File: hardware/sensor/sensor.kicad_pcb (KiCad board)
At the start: 2 copper layers, 88.9 x 68.6 mm, 12 parts

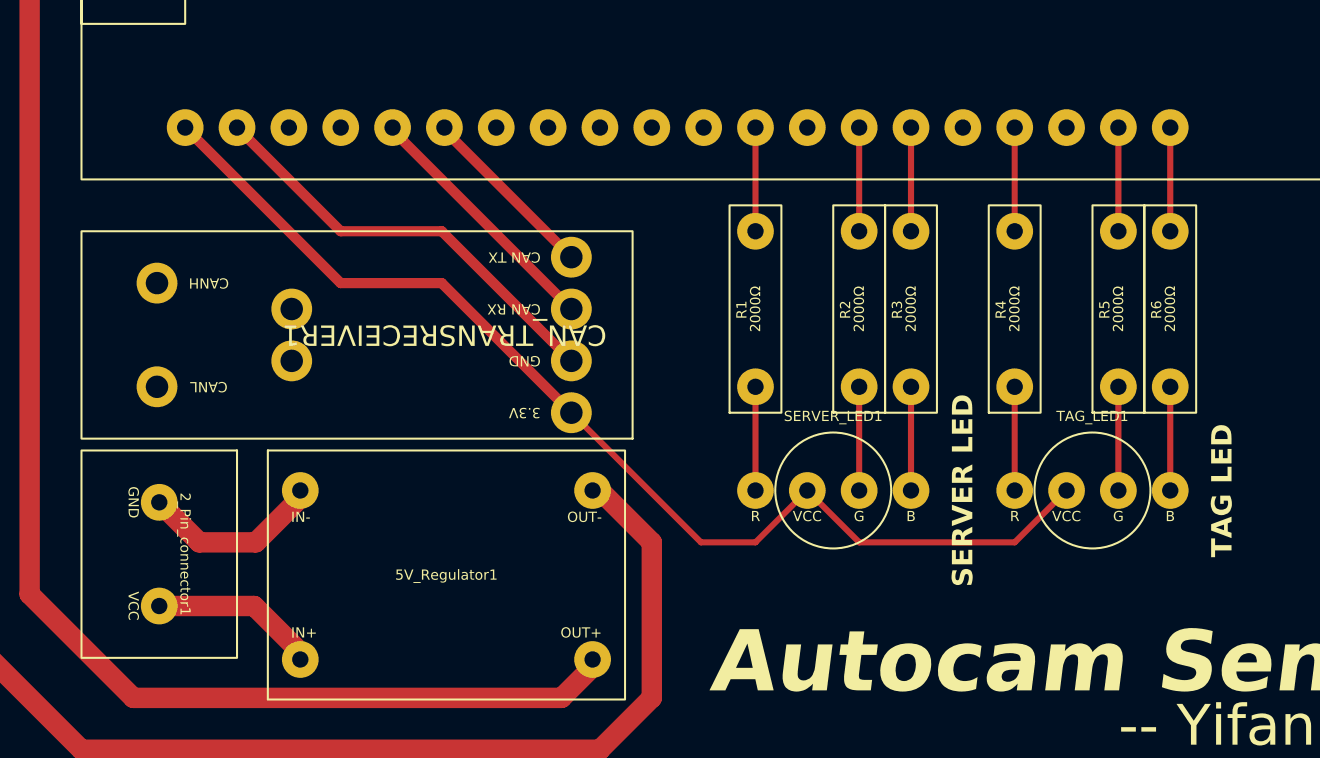
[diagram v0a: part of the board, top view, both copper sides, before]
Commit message: KiCad footprint library: Refactor footprint names.
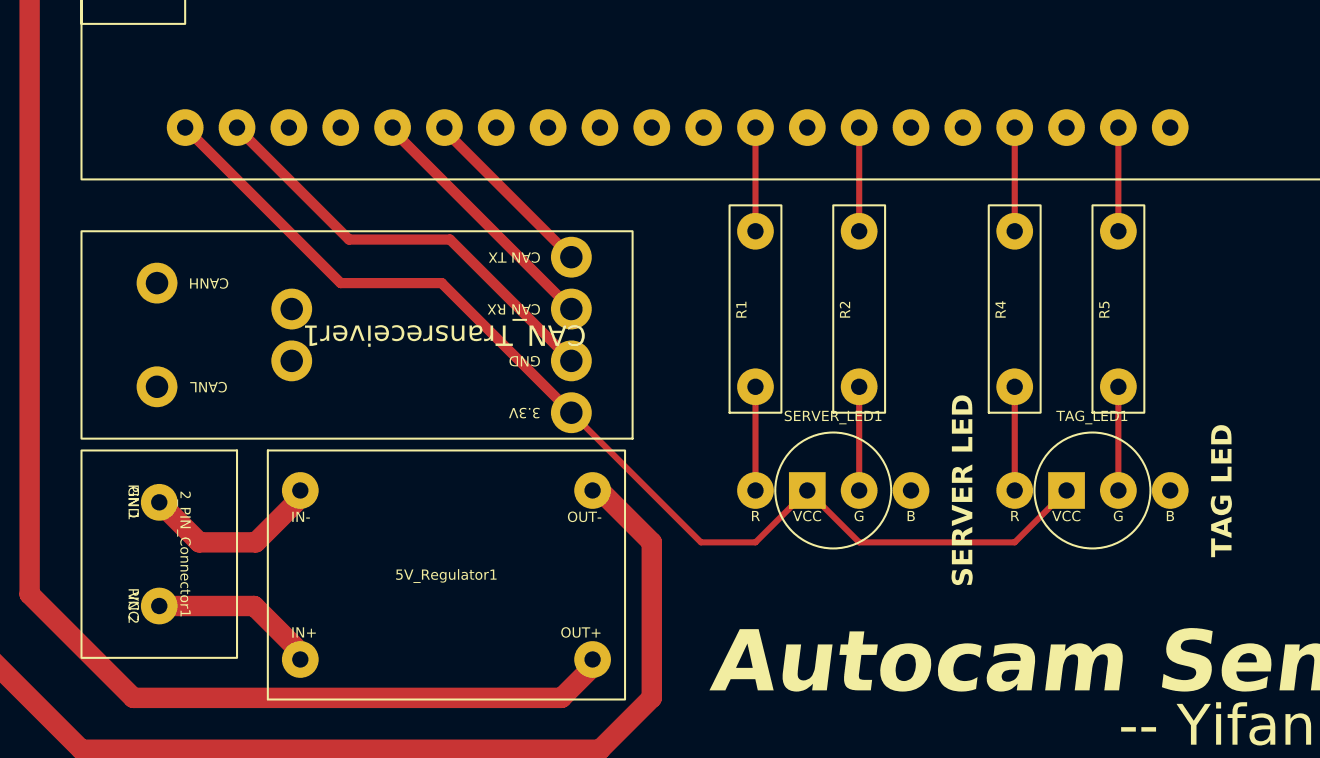
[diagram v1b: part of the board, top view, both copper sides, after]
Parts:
- removed R3, R6: 2000Ω, autocam:resistor
- 2_PIN_Connector1: renamed from 2_Pin_connector1; footprint autocam:2-pin connector -> Autocam:2-PIN Connector
- 5V_Regulator1: footprint autocam:MP1584EN 5V regulator -> Autocam:MP1584EN 5V Regulator
- CAN_Transreceiver1: renamed from CAN_TRANSRECEIVER1; footprint autocam:Waveshare CAN transreceiver -> Autocam:Waveshare CAN Transreceiver
- ESP32_UWB1: footprint autocam:esp32_uwb1000 -> Autocam:Makersfab ESP32 UWB
- R1, R2, R4, R5: footprint autocam:resistor -> Autocam:Simple Resistor
- SERVER_LED1, TAG_LED1: footprint autocam:Anode REB LED (round) -> Autocam:Anode RGB LED (Round)
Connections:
- ESP32_UWB1 pad 15: Net-(ESP32_UWB1-IO32) -> unconnected-(ESP32_UWB1-IO32-Pad15)
- ESP32_UWB1 pad 20: Net-(ESP32_UWB1-IO39) -> unconnected-(ESP32_UWB1-IO39-Pad20)
- SERVER_LED1 pad 4: Net-(SERVER_LED1-B) -> unconnected-(SERVER_LED1-B-Pad4)
- TAG_LED1 pad 4: Net-(TAG_LED1-B) -> unconnected-(TAG_LED1-B-Pad4)
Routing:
- net Net-(TAG_LED1-B): track 5.08 -> 0.00 mm
- net Net-(SERVER_LED1-B): track 5.08 -> 0.00 mm
- net Net-(ESP32_UWB1-IO39): track 5.08 -> 0.00 mm
- net Net-(ESP32_UWB1-IO32): track 5.08 -> 0.00 mm

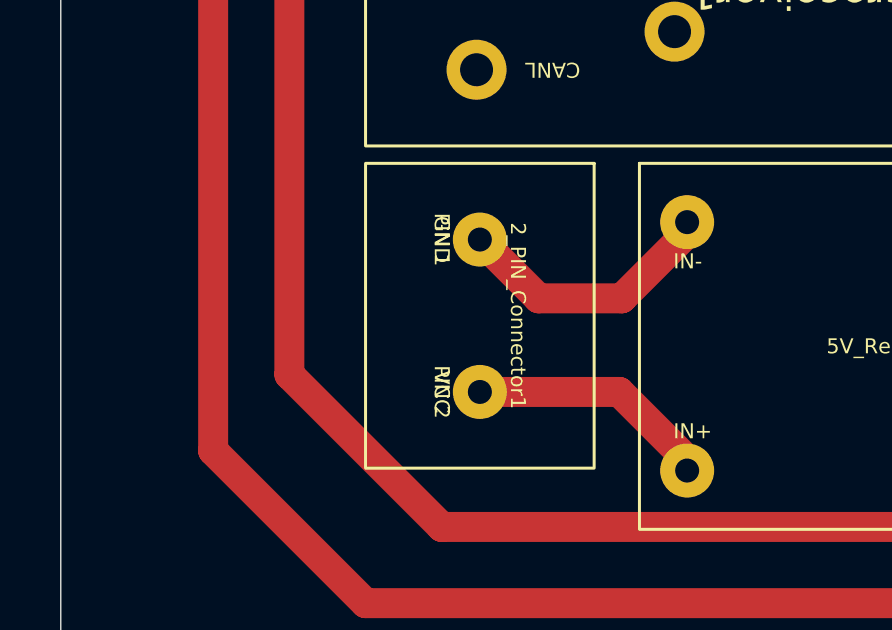
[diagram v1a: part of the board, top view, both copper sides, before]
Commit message: hardware/server: Add server PCB.
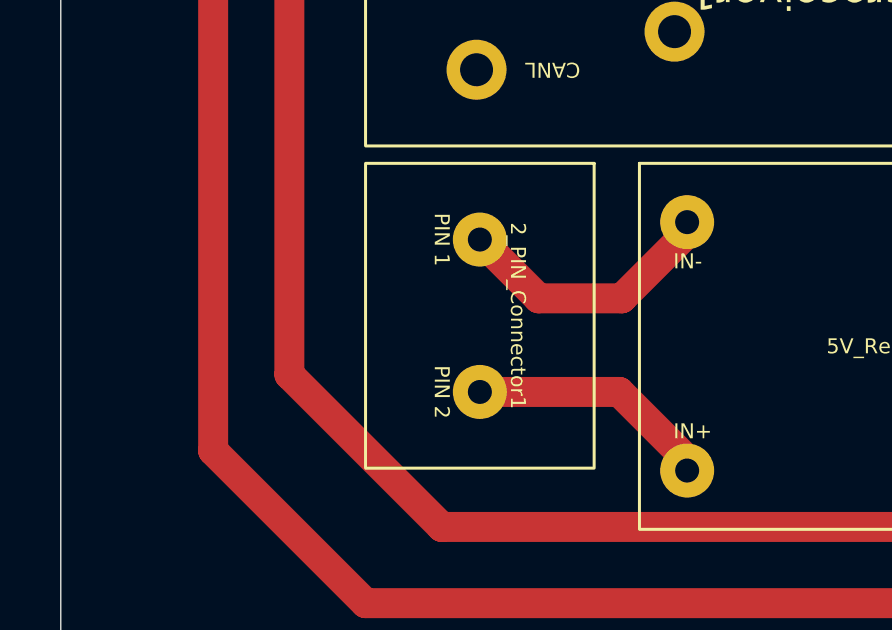
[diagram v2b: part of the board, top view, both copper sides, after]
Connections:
- SERVER_LED1 pad 1: Net-(SERVER_LED1-R) -> Net-(ESP32_UWB1-IO25)
- SERVER_LED1 pad 3: Net-(SERVER_LED1-G) -> Net-(ESP32_UWB1-IO27)
- TAG_LED1 pad 1: Net-(TAG_LED1-R) -> Net-(ESP32_UWB1-IO34)
- TAG_LED1 pad 3: Net-(TAG_LED1-G) -> Net-(ESP32_UWB1-IO36)

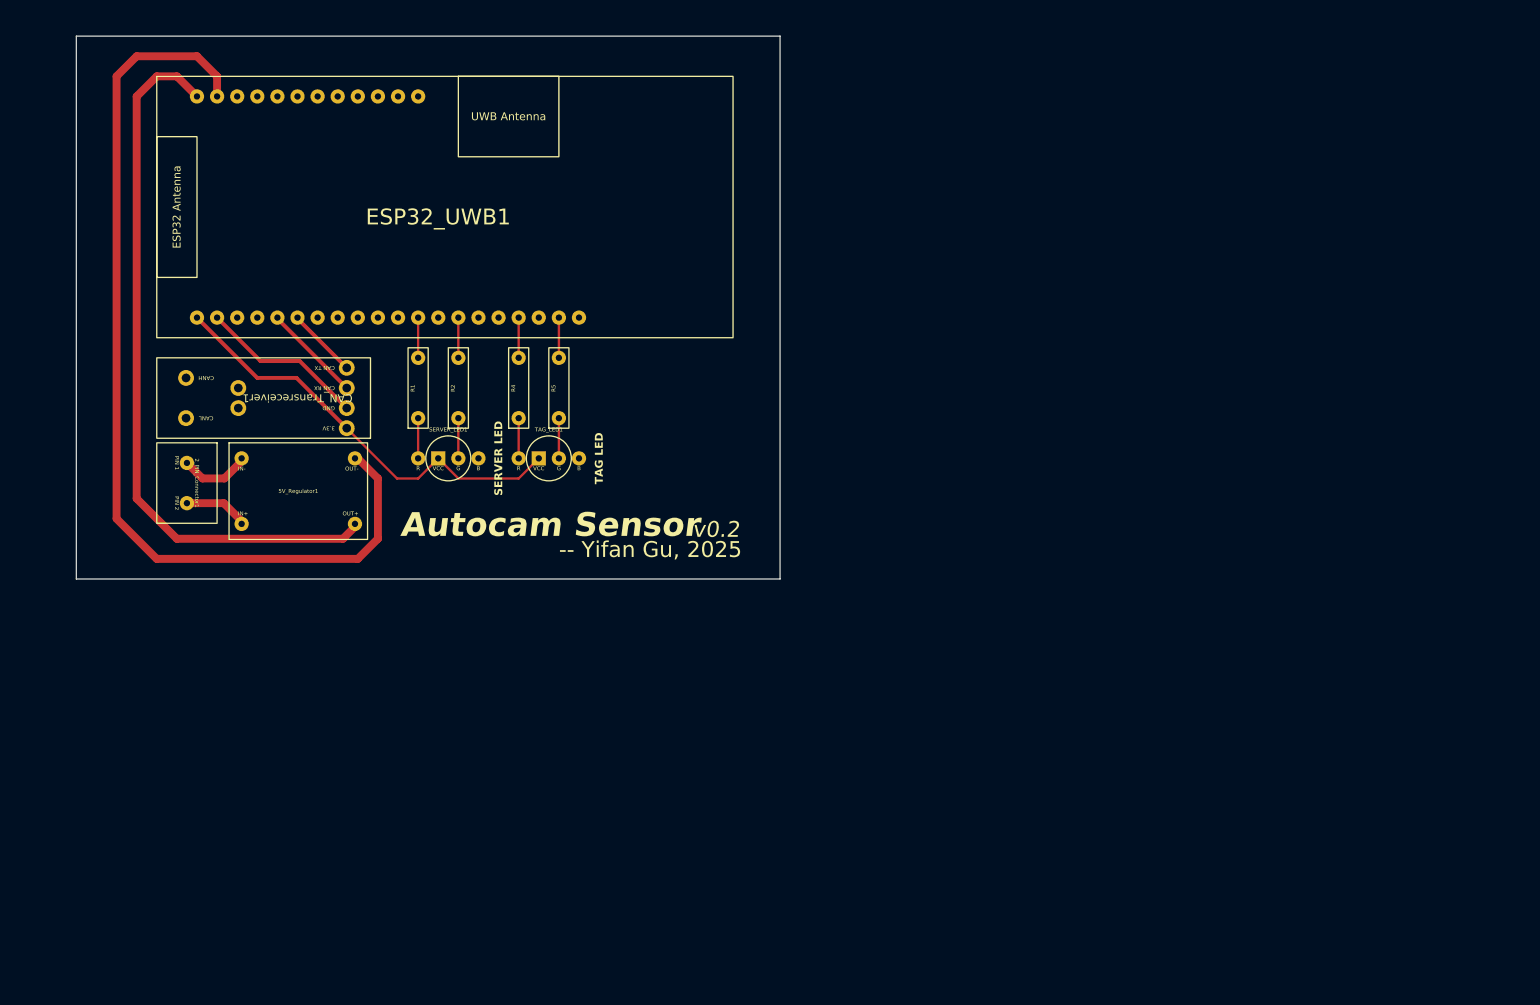
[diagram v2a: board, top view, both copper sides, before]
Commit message: hardware/tag: Add Autocam Tag PCB.
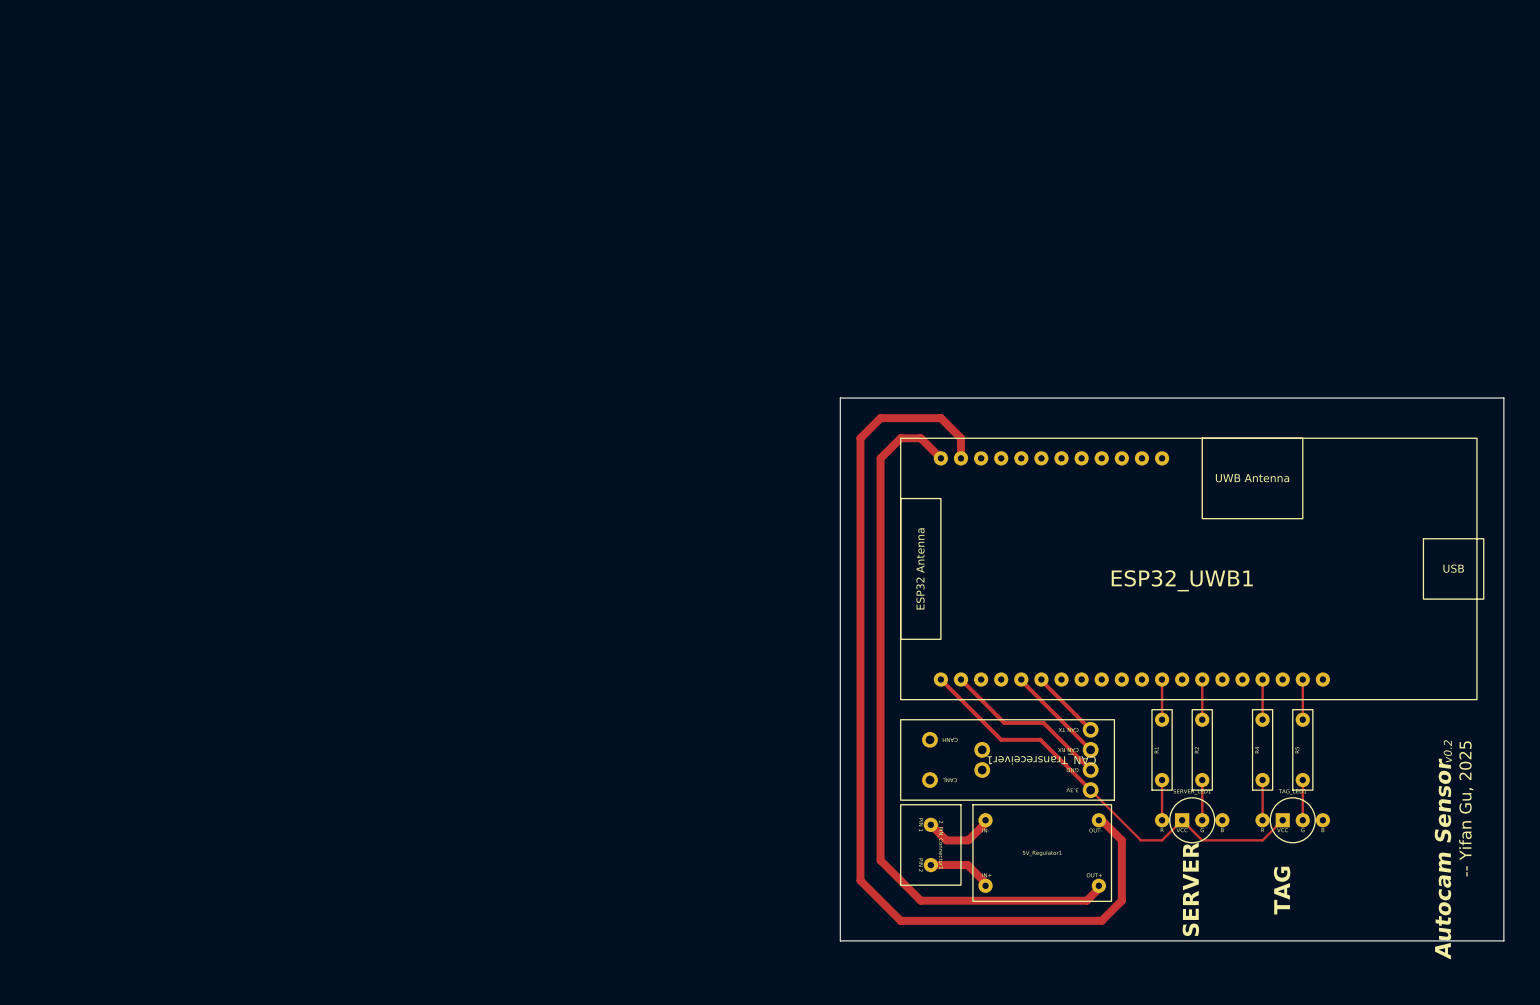
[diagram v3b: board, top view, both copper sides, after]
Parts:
- moved R5 104.5 mm to (177.8, 111.8)
- moved SERVER_LED1 104.5 mm to (163.8, 116.8)
- moved R1 104.5 mm to (160.0, 111.8)
- moved R4 104.5 mm to (172.7, 111.8)
- moved TAG_LED1 104.5 mm to (176.5, 116.8)
- moved 2_PIN_Connector1 104.5 mm to (127.0, 114.9)
- moved 5V_Regulator1 104.5 mm to (136.1, 114.9)
- moved CAN_Transreceiver1 104.5 mm to (127.0, 104.1)
- moved ESP32_UWB1 104.5 mm to (127.0, 68.6)
- moved R2 104.5 mm to (165.1, 111.8)
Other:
- board size 88.9 x 68.6 mm -> 83.8 x 68.6 mm
- board text added: "SERVER"
- board text added: "TAG"
- board text removed: "SERVER LED"
- board text removed: "TAG LED"

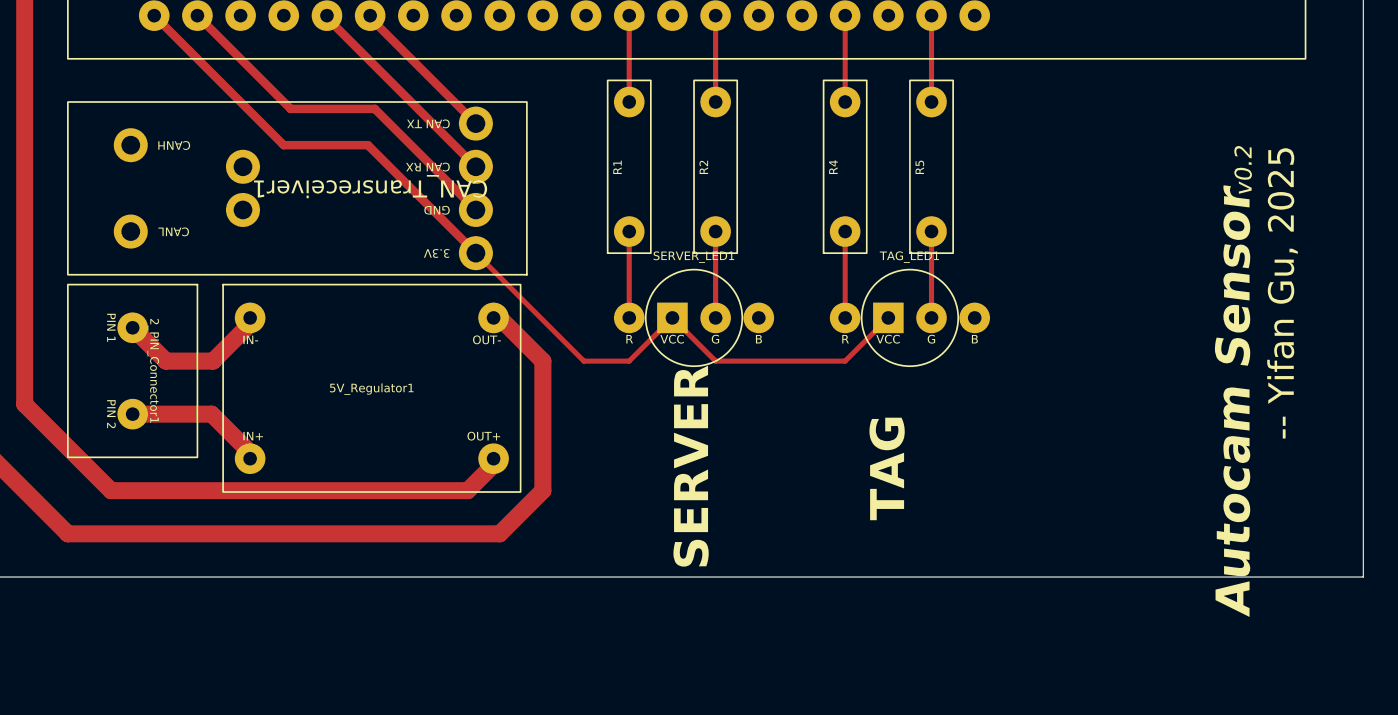
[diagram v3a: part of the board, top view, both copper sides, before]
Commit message: hardware: Add more footprint measurement.
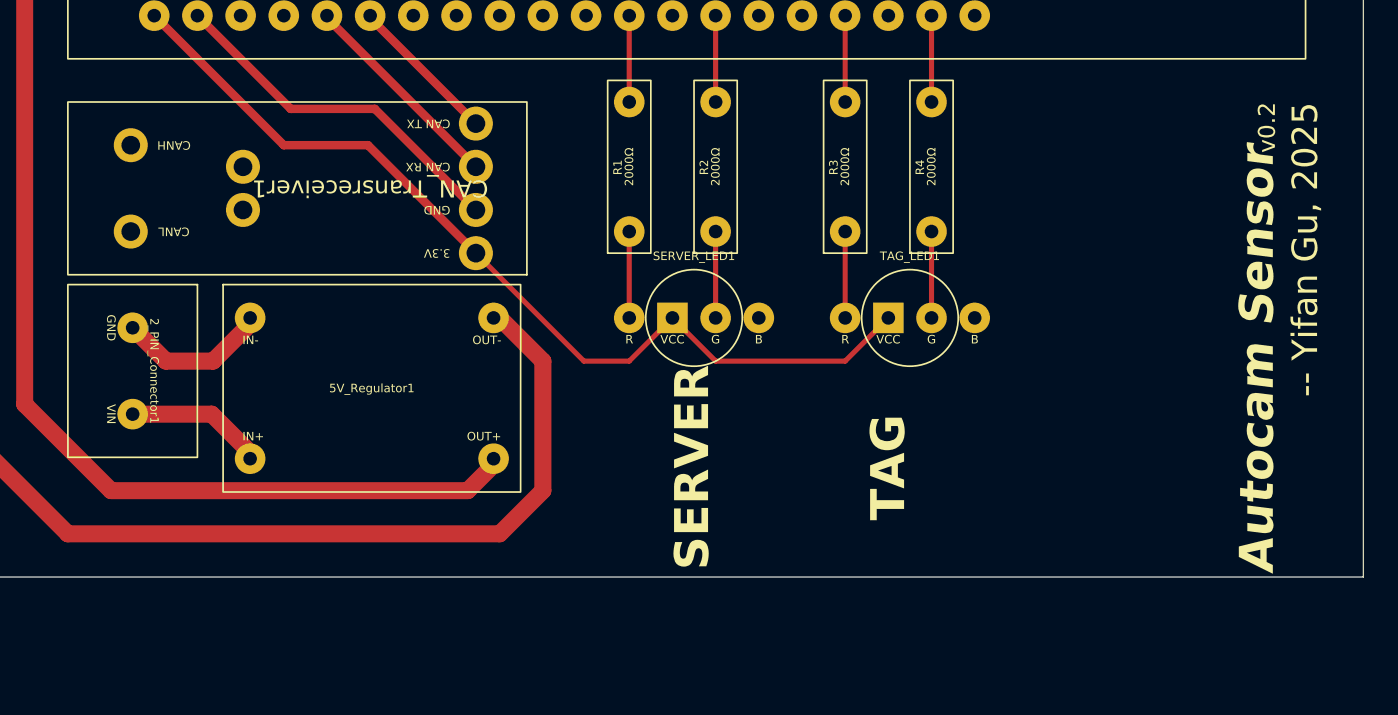
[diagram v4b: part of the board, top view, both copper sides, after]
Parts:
- removed R5: 2000Ω, Autocam:Simple Resistor
- added R3: 2000Ω, Autocam:Simple Resistor, F.Cu at (172.7, 111.8)
- moved R4 5.08 mm to (177.8, 111.8)
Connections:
- R4 pad 1: Net-(TAG_LED1-R) -> Net-(TAG_LED1-G)
- R4 pad 2: Net-(ESP32_UWB1-IO34) -> Net-(ESP32_UWB1-IO36)
- SERVER_LED1 pad 1: Net-(ESP32_UWB1-IO25) -> Net-(SERVER_LED1-R)
- SERVER_LED1 pad 3: Net-(ESP32_UWB1-IO27) -> Net-(SERVER_LED1-G)
- TAG_LED1 pad 1: Net-(ESP32_UWB1-IO34) -> Net-(TAG_LED1-R)
- TAG_LED1 pad 3: Net-(ESP32_UWB1-IO36) -> Net-(TAG_LED1-G)

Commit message: hardware: Add remote PCB.
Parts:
- SERVER_LED1: value ~ -> SERVER
- TAG_LED1: value ~ -> TAG
- moved R4 7.73 mm to (170.2, 110.5)
- moved R3 5.24 mm to (167.6, 110.5)
- moved R2 2.84 mm to (162.6, 110.5)
- moved R1 1.27 mm to (160.0, 110.5)
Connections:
- ESP32_UWB1 pad 13: unconnected-(ESP32_UWB1-IO26-Pad13) -> Net-(ESP32_UWB1-IO26)
- ESP32_UWB1 pad 14: Net-(ESP32_UWB1-IO27) -> unconnected-(ESP32_UWB1-IO27-Pad14)
- ESP32_UWB1 pad 15: unconnected-(ESP32_UWB1-IO32-Pad15) -> Net-(ESP32_UWB1-IO32)
- ESP32_UWB1 pad 16: unconnected-(ESP32_UWB1-IO33-Pad16) -> Net-(ESP32_UWB1-IO33)
- ESP32_UWB1 pad 17: Net-(ESP32_UWB1-IO34) -> unconnected-(ESP32_UWB1-IO34-Pad17)
- ESP32_UWB1 pad 19: Net-(ESP32_UWB1-IO36) -> unconnected-(ESP32_UWB1-IO36-Pad19)
- R2 pad 2: Net-(ESP32_UWB1-IO27) -> Net-(ESP32_UWB1-IO26)
- R3 pad 2: Net-(ESP32_UWB1-IO34) -> Net-(ESP32_UWB1-IO32)
- R4 pad 2: Net-(ESP32_UWB1-IO36) -> Net-(ESP32_UWB1-IO33)
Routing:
- net Net-(5V_Regulator1-OUT-): track 120.6 -> 114.9 mm
- net Net-(TAG_LED1-G): track 5.08 -> 10.3 mm
- net Net-(ESP32_UWB1-IO36): track 5.08 -> 0.00 mm
- net Net-(ESP32_UWB1-IO34): track 5.08 -> 0.00 mm
- net Net-(ESP32_UWB1-IO27): track 5.08 -> 0.00 mm
- net Net-(ESP32_UWB1-IO33): track 0.00 -> 3.81 mm
- net Net-(ESP32_UWB1-IO32): track 0.00 -> 3.81 mm
- net Net-(ESP32_UWB1-IO26): track 0.00 -> 3.81 mm
- net Net-(TAG_LED1-R): track 5.08 -> 8.45 mm
- net Net-(SERVER_LED1-G): track 5.08 -> 7.40 mm
- net Net-(2_PIN_Connector1-Pin_1): track 9.13 -> 7.15 mm
- net Net-(SERVER_LED1-R): track 5.08 -> 6.35 mm
- net Net-(ESP32_UWB1-IO25): track 5.08 -> 3.81 mm
- net Net-(5V_Regulator1-OUT+): track 91.3 -> 92.5 mm
